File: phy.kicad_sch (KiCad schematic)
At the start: 30 parts, among them J8 RJ45_HanRun_HR911105A, U201 LAN8720A, X201 50M

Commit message: Modif commande v2.0
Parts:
- U201: footprint Package_DFN_QFN:VQFN-24-1EP_4x4mm_P0.5mm_EP2.5x2.5mm_ThermalVias -> Package_DFN_QFN:VQFN-24-1EP_4x4mm_P0.5mm_EP2.5x2.5mm
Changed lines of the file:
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@@
       (effects (font (size 1.27 1.27)) (justify left))
     )
-    (property "Footprint" "Package_DFN_QFN:VQFN-24-1EP_4x4mm_P0.5mm_EP2.5x2.5mm_ThermalVias" (at 132.08 116.84 0)
+    (property "Footprint" "Package_DFN_QFN:VQFN-24-1EP_4x4mm_P0.5mm_EP2.5x2.5mm" (at 132.08 116.84 0)
       (effects (font (size 1.27 1.27)) (justify left) hide)
     )

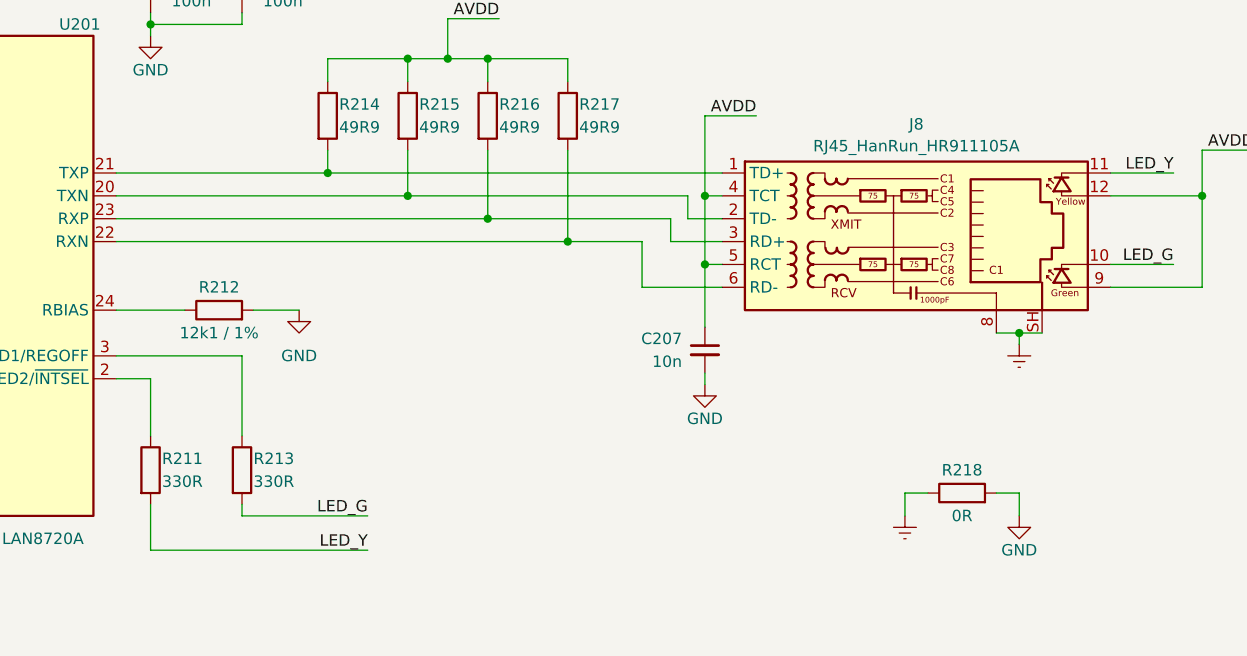
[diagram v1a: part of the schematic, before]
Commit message: Mise a jour resistance puissance LED
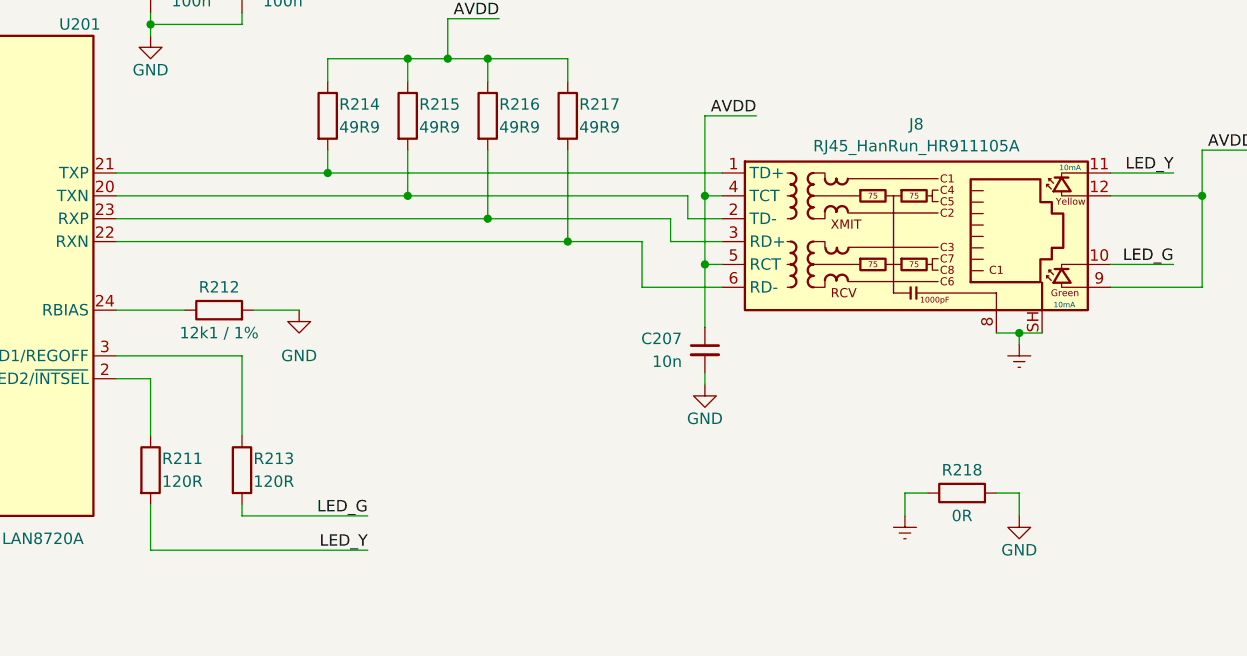
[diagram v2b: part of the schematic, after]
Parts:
- R211, R213: value 330R -> 120R
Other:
- note added: "10mA"
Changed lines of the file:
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@@
     (stroke (width 0) (type default))
+  )
+  (text "10mA" (at 253.365 77.47 0)
+    (effects (font (size 0.6 0.6)) (justify left bottom))
+  )
+  (text "10mA" (at 252.73 92.71 0)
+    (effects (font (size 0.6 0.6)) (justify left bottom))
   )
   (text "LAN8720 Module" (at 16.51 21.59 0)
@@
       (effects (font (size 1.27 1.27)) (justify left))
     )
-    (property "Value" "330R" (at 153.67 111.76 0)
+    (property "Value" "120R" (at 153.67 111.76 0)
       (effects (font (size 1.27 1.27)) (justify left))
     )
@@
       (effects (font (size 1.27 1.27)) (justify left))
     )
-    (property "Value" "330R" (at 163.83 111.76 0)
-      (effects (font (size 1.27 1.27)) (justify left))
-    )
+    (property "Value" "120R" (at 163.83 111.76 0)
+      (effects (font (size 1.27 1.27)) (justify left))
+    )

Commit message: Mise a jour 1er assemblage
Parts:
- R211, R213: LCSC# C105878 -> C114245; Mouser# 603-RC0805FR-07330RL -> 603-RC0805FR-07120RL
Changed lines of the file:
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@@
       (effects (font (size 1.27 1.27)) hide)
     )
-    (property "LCSC#" "C105878" (at 152.4 110.49 0)
-      (effects (font (size 1.27 1.27)) hide)
-    )
-    (property "Mouser#" "603-RC0805FR-07330RL" (at 152.4 110.49 0)
+    (property "LCSC#" "C114245" (at 152.4 110.49 0)
+      (effects (font (size 1.27 1.27)) hide)
+    )
+    (property "Mouser#" "603-RC0805FR-07120RL" (at 152.4 110.49 0)
       (effects (font (size 1.27 1.27)) hide)
     )
@@
       (effects (font (size 1.27 1.27)) hide)
     )
-    (property "LCSC#" "C105878" (at 162.56 110.49 0)
-      (effects (font (size 1.27 1.27)) hide)
-    )
-    (property "Mouser#" "603-RC0805FR-07330RL" (at 162.56 110.49 0)
-      (effects (font (size 1.27 1.27)) hide)
-    )
+    (property "LCSC#" "C114245" (at 162.56 110.49 0)
+      (effects (font (size 1.27 1.27)) hide)
+    )
+    (property "Mouser#" "603-RC0805FR-07120RL" (at 162.56 110.49 0)
+      (effects (font (size 1.27 1.27)) hide)
+    )
